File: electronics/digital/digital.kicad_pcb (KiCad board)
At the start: 2 copper layers, 58 parts, among them J1 USB_A, J2 USB_A, J3 RJ45, P1 POWER_IN, P10 AMP_POWER_OUT, P11 CONTROL, P2 3V3_IN, P3 USB_CABLE, P4 USB_CABLE, P5 NETWORK_CABLE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

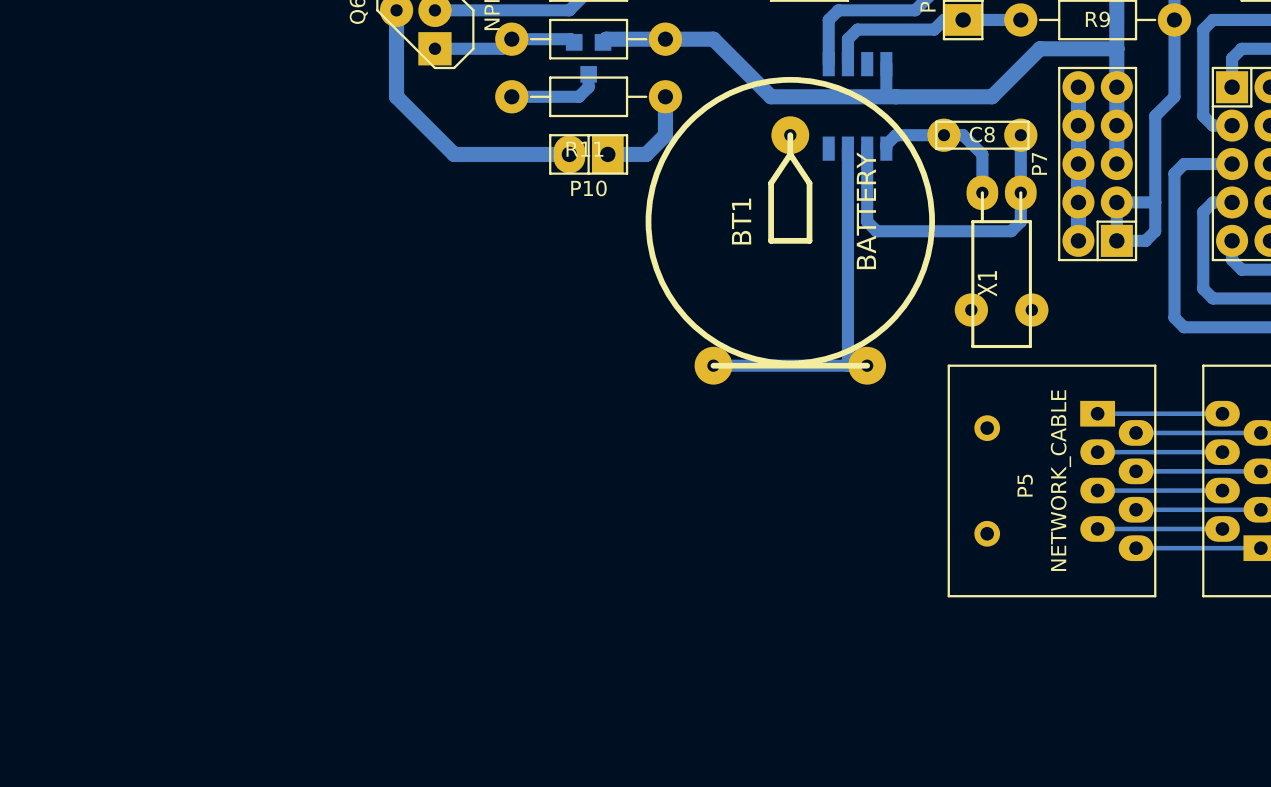
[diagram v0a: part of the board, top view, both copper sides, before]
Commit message: add lightmeter to schematic
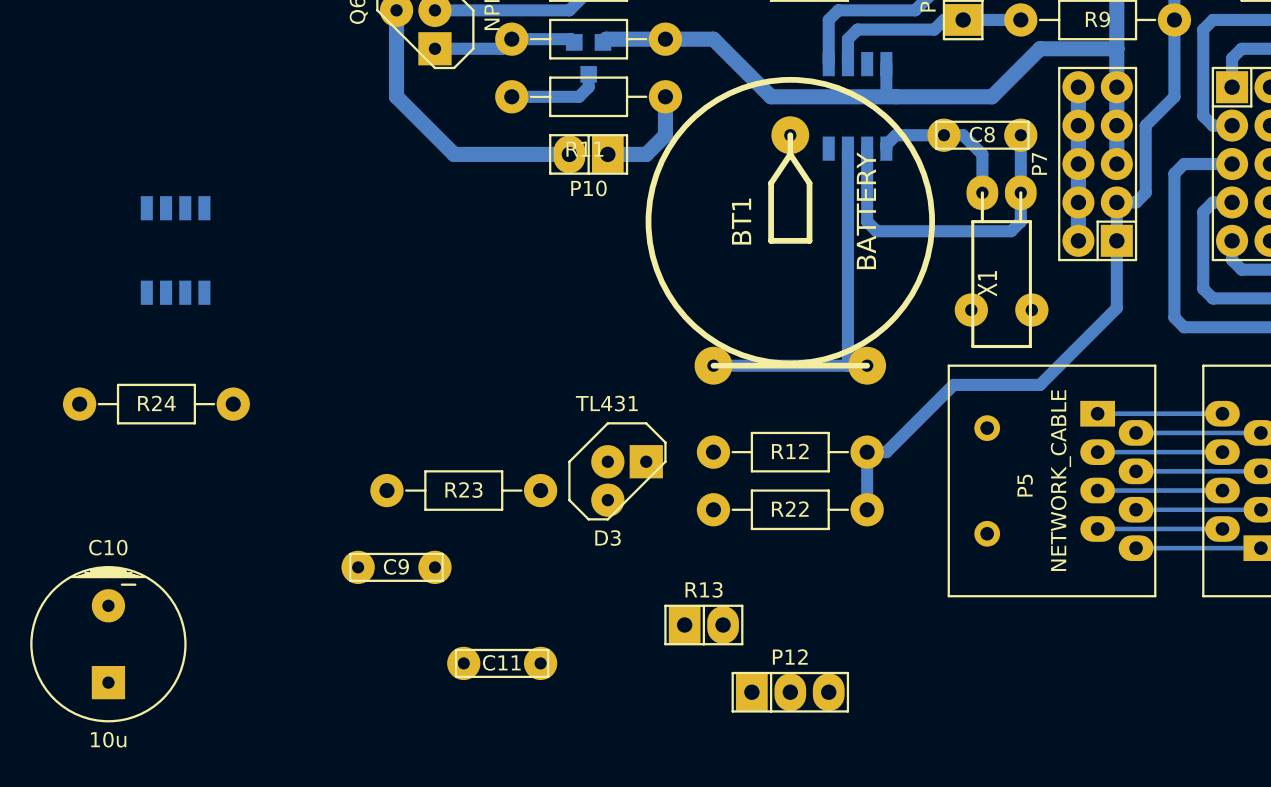
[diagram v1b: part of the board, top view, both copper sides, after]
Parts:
- added C10: 10u, Capacitors_ThroughHole:Capacitor10x16RM5, F.Cu at (171.4, 149.2)
- added C11: 100n, Capacitors_ThroughHole:Capacitor6MMDiscRM5, F.Cu at (197.5, 150.5)
- added C9: 100n, Capacitors_ThroughHole:Capacitor6MMDiscRM5, F.Cu at (190.5, 144.1)
- added D3: TL431, Discret:TO92-123, F.Cu at (205.7, 138.4)
- added P12: ADC, Pin_Headers:Pin_Header_Straight_1x03, F.Cu at (216.5, 152.4)
- added R12: 10k, Resistors_ThroughHole:Resistor_Horizontal_RM10mm, F.Cu at (216.5, 136.5)
- added R13: Photores, Pin_Headers:Pin_Header_Straight_1x02, F.Cu at (210.8, 148.0)
- added R22: 10k, Resistors_ThroughHole:Resistor_Horizontal_RM10mm, F.Cu at (216.5, 140.3)
- added R23: 2.2k, Resistors_ThroughHole:Resistor_Horizontal_RM10mm, F.Cu at (194.9, 139.1)
- added R24: 10k, Resistors_ThroughHole:Resistor_Horizontal_RM10mm, F.Cu at (174.6, 133.3)
- added U2: MCP3001, Power_Integrations:SO-8, B.Cu at (175.9, 123.2)
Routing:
- net +3.3VP: track 35.6 -> 58.9 mm

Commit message: fuck 3v3
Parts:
- moved C10 36.6 mm to (201.9, 128.9), turned to 270 degrees
- moved U2 31.0 mm to (203.2, 137.8)
- moved D3 21.4 mm to (184.8, 134.0), turned to 90 degrees
- moved R24 17.3 mm to (191.8, 135.3), turned to 90 degrees
- moved R13 14.3 mm to (196.8, 144.8), turned to 180 degrees
- moved R12 13.9 mm to (203.2, 140.3)
- moved P12 13.2 mm to (205.7, 144.8), turned to 180 degrees
- moved R23 8.64 mm to (203.2, 136.5), turned to 180 degrees
- moved R22 3.81 mm to (216.5, 136.5)
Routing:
- net Net-(C9-Pad1): track 0.00 -> 8.55 mm
- net +3.3VP: track 58.9 -> 52.3 mm

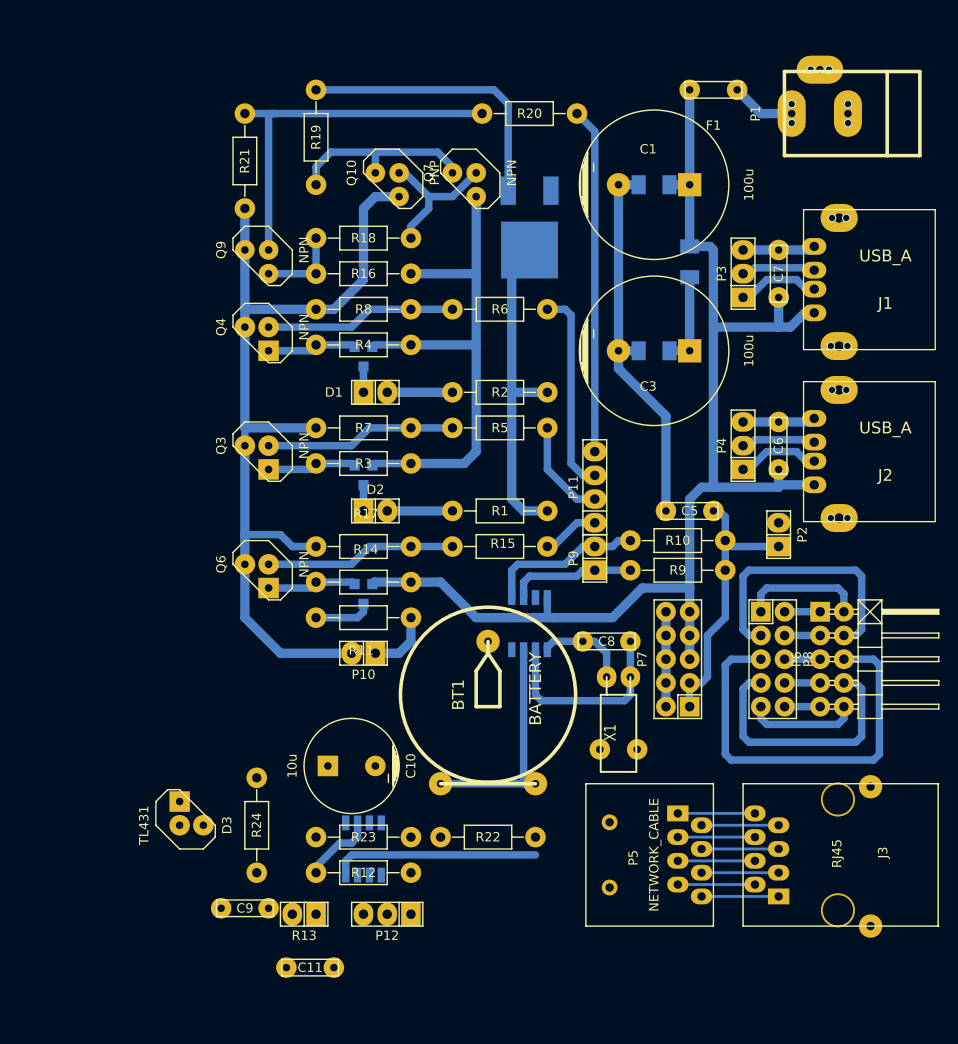
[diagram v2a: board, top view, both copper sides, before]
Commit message: finish routing of lightmeter
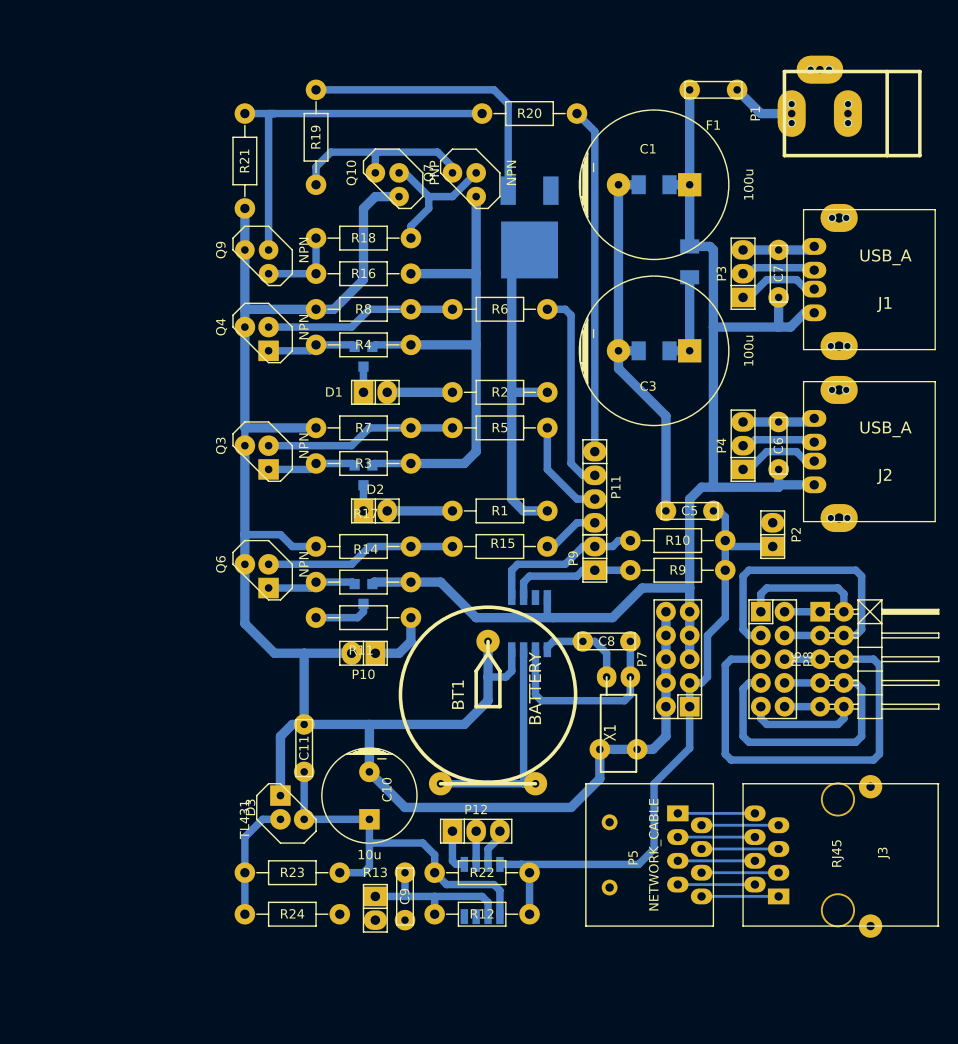
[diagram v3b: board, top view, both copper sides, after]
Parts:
- moved C11 23.5 mm to (196.8, 127.0), turned to 90 degrees
- moved C9 17.2 mm to (207.6, 142.9), turned to 270 degrees
- moved U2 13.5 mm to (215.9, 142.2), turned to 180 degrees
- moved R12 13.5 mm to (215.9, 144.8)
- moved P12 13.0 mm to (215.3, 135.9), turned to 0 degrees
- moved D3 10.8 mm to (195.6, 133.3)
- moved R24 10.3 mm to (195.6, 144.8), turned to 0 degrees
- moved R23 8.52 mm to (195.6, 140.3)
- moved R13 7.65 mm to (204.5, 144.1), turned to 270 degrees
- moved R22 3.86 mm to (215.9, 140.3)
- moved C10 3.70 mm to (203.8, 132.1), turned to 0 degrees
- moved P2 0.64 mm to (247.0, 104.1)
- turned P11 to 270 degrees
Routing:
- net GND: track 165.6 -> 261.8 mm
- net Net-(C10-Pad1): track 0.00 -> 40.6 mm
- net /LED_PWM: track 4.60 -> 37.0 mm
- net /AMP_SEL: track 38.5 -> 6.13 mm
- net +3.3VP: track 52.3 -> 69.2 mm
- net Net-(D3-Pad2): track 0.00 -> 12.9 mm
- net Net-(C9-Pad1): track 8.55 -> 18.3 mm
- net /LED_SEL_2: track 5.72 -> 10.8 mm
- net /LED_SEL_1: track 26.9 -> 21.7 mm
- net Net-(P12-Pad1): track 0.00 -> 4.60 mm
- net Net-(P12-Pad3): track 0.00 -> 4.08 mm
- net Net-(P12-Pad2): track 0.00 -> 3.56 mm

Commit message: fuck.
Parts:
- moved F1 8.64 mm to (245.7, 63.5), turned to 270 degrees
- moved P1 2.69 mm to (257.2, 61.0)
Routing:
- net +5V: track 134.5 -> 132.3 mm
- net Net-(F1-Pad1): track 6.89 -> 5.21 mm
- added copper zone on B.Cu, net GND

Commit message: working on polygon
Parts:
- moved L1 4.45 mm to (238.1, 70.5)
- moved C1 1.27 mm to (234.3, 65.4)
- moved C2 1.27 mm to (234.3, 65.4)
- moved C3 1.27 mm to (234.3, 85.7)
- moved C4 1.27 mm to (234.3, 85.7)
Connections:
- J3 pad Hole: (no net) -> GND
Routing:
- net GND: track 261.8 -> 212.6 mm
- net /LED_VCC: track 67.3 -> 95.8 mm, vias 0 -> 2
- net +5V: track 132.3 -> 133.5 mm

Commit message: finish polygon
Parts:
- moved P2 0.64 mm to (247.0, 103.5)
- moved P6 0.63 mm to (253.4, 116.8)
- moved P8 0.63 mm to (247.0, 116.8)
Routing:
- net GND: track 212.6 -> 213.2 mm

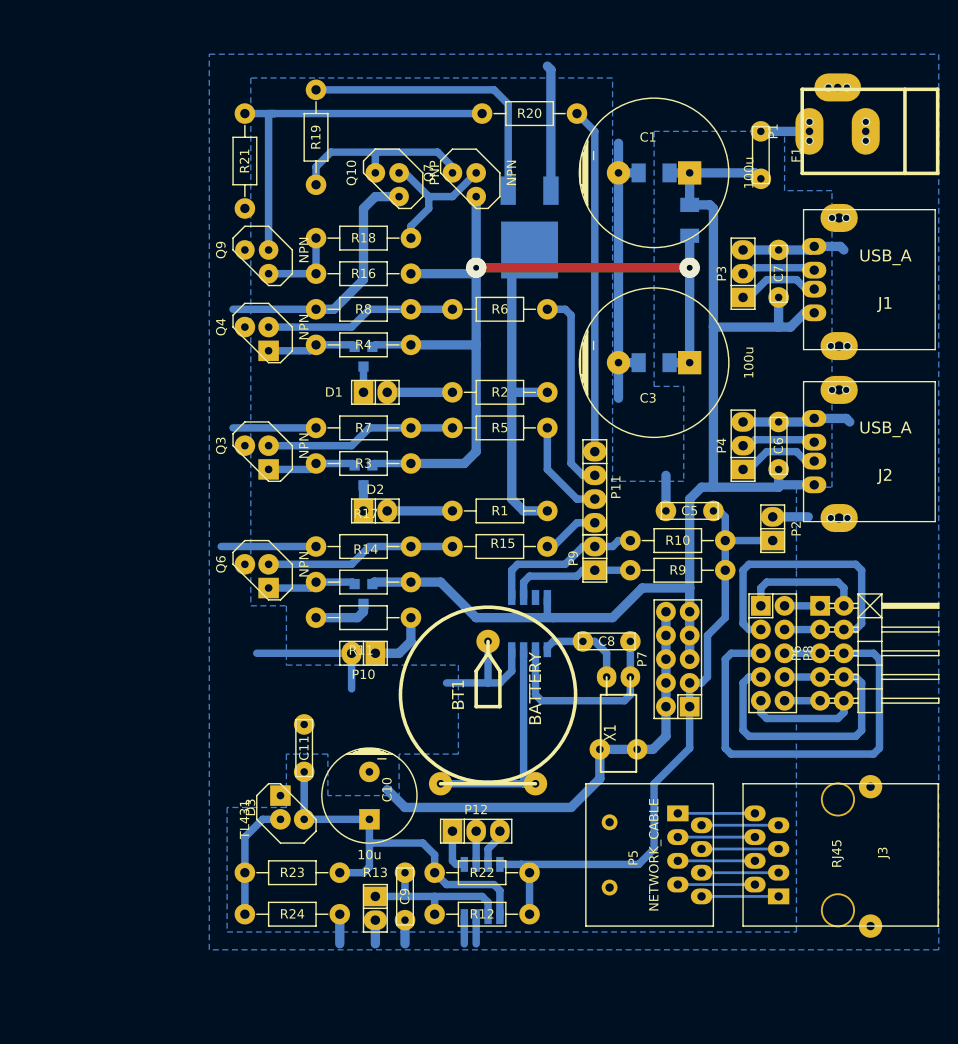
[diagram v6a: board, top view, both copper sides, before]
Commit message: move some resistors, add holes
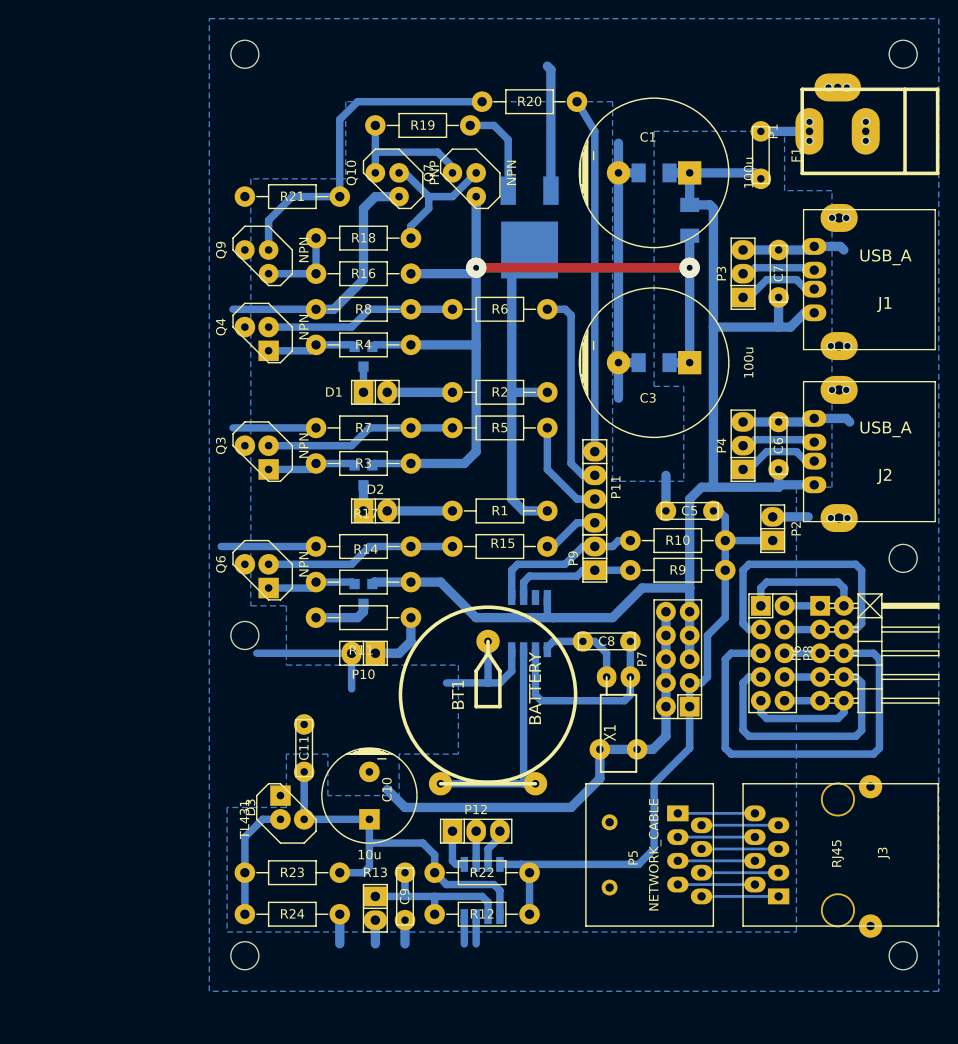
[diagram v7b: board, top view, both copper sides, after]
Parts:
- added MountingHole_3mm: VAL**, Mounting_Holes:MountingHole_3mm, F.Cu at (261.0, 106.7)
- added MountingHole_3mm: VAL**, Mounting_Holes:MountingHole_3mm, F.Cu at (261.0, 149.2)
- added MountingHole_3mm: VAL**, Mounting_Holes:MountingHole_3mm, F.Cu at (190.5, 52.7)
- added MountingHole_3mm: VAL**, Mounting_Holes:MountingHole_3mm, F.Cu at (190.5, 114.9)
- added MountingHole_3mm: VAL**, Mounting_Holes:MountingHole_3mm, F.Cu at (190.5, 149.2)
- added MountingHole_3mm: VAL**, Mounting_Holes:MountingHole_3mm, F.Cu at (261.0, 52.7)
- moved R19 11.5 mm to (209.6, 60.3), turned to 180 degrees
- moved R21 6.35 mm to (195.6, 67.9), turned to 0 degrees
- moved R20 1.27 mm to (221.0, 57.8)
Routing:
- net Net-(Q8-PadG): track 30.8 -> 10.5 mm
- net Net-(Q10-Pad1): track 20.7 -> 14.6 mm
- net Net-(Q9-Pad2): track 40.6 -> 36.1 mm
- net /LED_PWM: track 37.0 -> 38.0 mm
